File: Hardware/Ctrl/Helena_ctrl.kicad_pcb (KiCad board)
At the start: 2 copper layers, 38 x 18 mm, 41 parts, among them P1 CONN_01X06, P2 CONN_01X04, Q1 BC857C, SW1 SW_PUSH, U1 antenna-gnd, U2 nrf51822-qfax, U3 MPU-6050, Y1 16MHz

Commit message: updated control board
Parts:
- removed C10, C7: 22p, rt_device:C_0603_THERMaL_RELIEF
- removed C11, C12, C3, C4: 100n, rt_device:C_0603_THERMaL_RELIEF
- removed C5: 1p0, rt_device:C_0603_THERMaL_RELIEF
- removed C6: 1n, rt_device:C_0603_THERMaL_RELIEF
- removed C8: 2p2, rt_device:C_0603_THERMaL_RELIEF
- removed C9: 2n2, rt_device:C_0603_THERMaL_RELIEF
- removed L1: 3n3, rt_device:C_0603_THERMaL_RELIEF
- removed L2: 4n7, rt_device:C_0603_THERMaL_RELIEF
- removed L3: 10n, rt_device:C_0603_THERMaL_RELIEF
- removed Q1: BC857C, TO_SOT_Packages_SMD:SOT-23
- removed U1: antenna-gnd, rt_antennas:MML_R302.302.000
- removed Y1: 16MHz, rt_XTAL:XTAL_MT_3.2mm_x_2.5mm
- added D2: LED_BLUE, rt_device:C_0603_THERMaL_RELIEF, F.Cu at (54.1, 148.5)
- added FB2: FB, rt_device:C_0603_THERMaL_RELIEF, B.Cu at (42.4, 155.7)
- C1: value dnp -> 2u2/16
- C2: value 1p5 -> 100n
- D1: value Double_LED -> LED_RED; footprint rt_leds:Duo-Led_0603 -> rt_device:C_0603_THERMaL_RELIEF
- P2: value CONN_01X04 -> CONN_02X05; footprint rt_Pin_Header:Pin_Header_Straight_1x04_Pitch1.27mm -> rt_Pin_Header:Pin_Header_Straight_2x05_Pitch1.27mm
- U2: value nrf51822-qfax -> nrf51822-04AT_Module; footprint Housings_DFN_QFN:UQFN-48-1EP_6x6mm_Pitch0.4mm -> WT51822-S4AT
- moved C13 25.6 mm to (36.5, 150.7), turned to 180 degrees
- moved C15 25.0 mm to (36.5, 149.1), turned to 180 degrees
- moved C17 24.3 mm to (39.2, 142.1), turned to 180 degrees
- moved U3 20.8 mm to (39.5, 145.6), turned to 180 degrees
- moved FB1 19.9 mm to (39.5, 150.7), turned to 180 degrees
- moved R2 19.6 mm to (38.4, 153.4)
- moved C14 19.1 mm to (39.5, 149.1), turned to 0 degrees
- moved R1 19.1 mm to (39.2, 155.7), turned to 180 degrees
- moved C16 16.8 mm to (40.0, 153.4)
- moved R3 14.0 mm to (42.5, 150.7), turned to 0 degrees
- moved R4 12.8 mm to (54.1, 154.5), turned to 90 degrees
- moved R5 12.6 mm to (42.5, 149.1), turned to 0 degrees
- moved U2 11.7 mm to (58.8, 150.4), turned to 90 degrees
- moved P2 9.83 mm to (48.9, 143.2), turned to 270 degrees
- moved D1 8.89 mm to (54.1, 151.5), turned to 270 degrees
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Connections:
- D1 pad 1: GND -> /~LED_RED~/LED_BLUE
- P2 pad 2: /SWDCLK -> /SWDIO
- P2 pad 4: /SWDIO -> /SWDCLK
- R4 pad 1: /LED_RED -> +3V3
- R4 pad 2: Net-(D1-Pad4) -> Net-(D1-Pad2)
- R7 pad 1: /LED_BLUE -> Net-(D2-Pad1)
- R7 pad 2: Net-(D1-Pad2) -> GND
- U2 pad 1: +3V3 -> Net-(C1-Pad1)
- U2 pad 10: /VIN_ADC -> /SWDIO
- U2 pad 11: Net-(U2-Pad11) -> /SWDCLK
- U2 pad 12: +3V3 -> GND
- U2 pad 15: Net-(U2-Pad15) -> GND
- U2 pad 2: Net-(U2-Pad2) -> GND
- U2 pad 3: Net-(U2-Pad3) -> /VIN_ADC
- U2 pad 4: Net-(U2-Pad4) -> /SDA
- U2 pad 5: Net-(U2-Pad5) -> /SCL
- U2 pad 6: Net-(U2-Pad6) -> /MPU_INT
- U2 pad 7: Net-(U2-Pad7) -> /BUTTON
- U2 pad 8: Net-(U2-Pad8) -> /BDEP_RX
- U2 pad 9: Net-(U2-Pad9) -> /~LED_RED~/LED_BLUE
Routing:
- net GND: track 159.0 -> 98.3 mm, vias 75 -> 39
- net /LED_RED: track 20.9 -> 0.00 mm, vias 1 -> 0
- net +3V3: track 57.5 -> 41.9 mm
- net /~LED_RED~/LED_BLUE: track 0.00 -> 11.0 mm, vias 0 -> 1
- net Net-(D1-Pad2): track 10.6 -> 1.48 mm
- net VPP: track 10.8 -> 19.7 mm, vias 1 -> 0
- net Net-(C10-Pad1): track 8.89 -> 0.00 mm
- net /BDEP_TX: track 8.40 -> 0.00 mm, vias 1 -> 0
- net /BUTTON: track 16.8 -> 25.1 mm, vias 1 -> 3
- net Net-(D1-Pad4): track 8.04 -> 0.00 mm
- net Net-(C7-Pad1): track 7.74 -> 0.00 mm
- net /LED_BLUE: track 7.06 -> 0.00 mm, vias 1 -> 0
- net Net-(C9-Pad1): track 6.09 -> 0.00 mm
- net /SDA: track 26.3 -> 20.9 mm, vias 1 -> 0
- net /SWDCLK: track 5.44 -> 10.0 mm
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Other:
- board text added: "1"
- board text added: "10pin ARM"
- board text added: "RT1703"
- board text added: "Wireless Ctrl. Rev 2.2"
- board text removed: "RT1612"
- board text removed: "SWDIO GND SWDCLK +3V3"
- board text removed: "Wireless Ctrl. Rev 2.1"

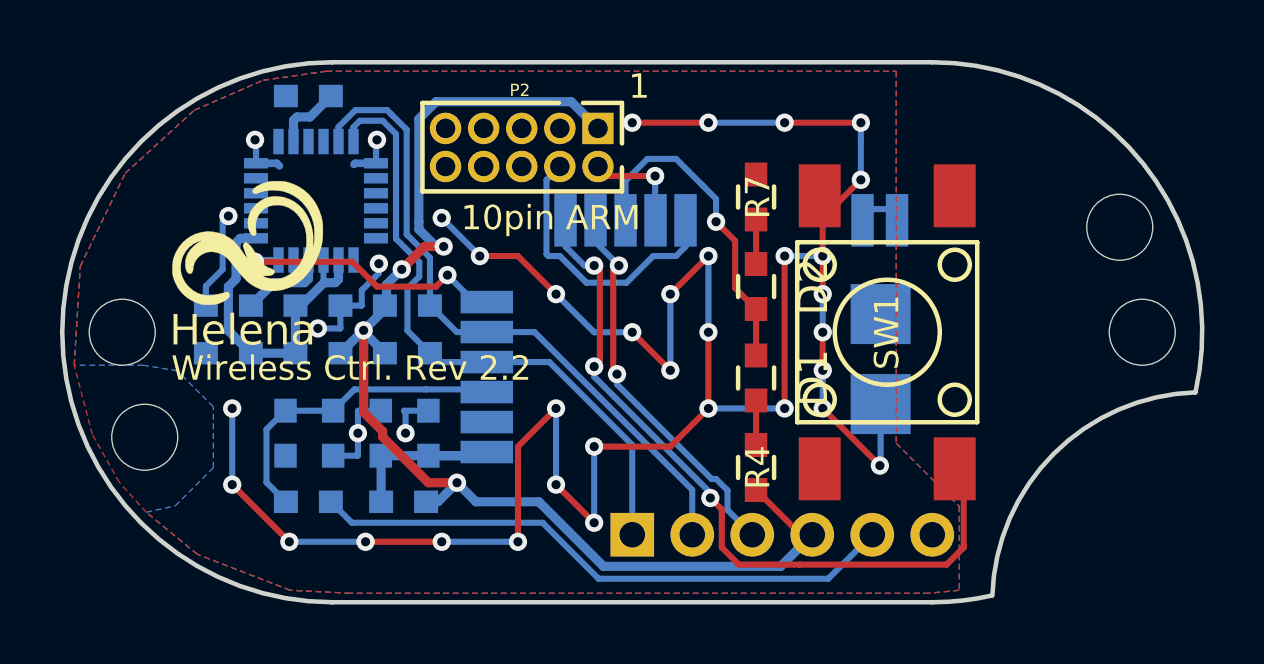
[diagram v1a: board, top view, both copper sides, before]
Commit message: Hardware update for better compatibility with KD2 style lights
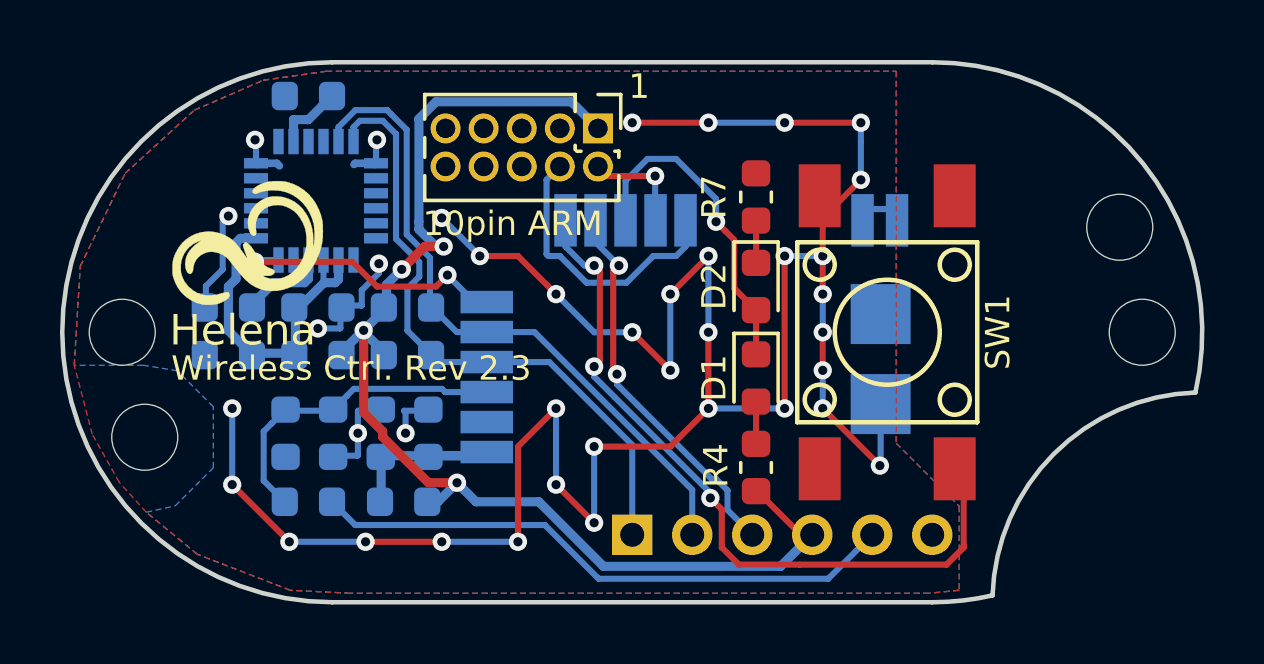
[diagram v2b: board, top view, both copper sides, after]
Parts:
- removed P1: CONN_01X06, rt_Pin_Header:Pin_Header_Straight_1x06_2.00_Pitch
- removed P2: CONN_02X05, rt_Pin_Header:Pin_Header_Straight_2x05_Pitch1.27mm
- added J1: CONN_01X06, Connector_PinHeader_2.00mm:PinHeader_1x06_P2.00mm_Vertical, B.Cu at (50.0, 156.8)
- added J2: CONN_02X05, Connector_PinHeader_1.27mm:PinHeader_2x05_P1.27mm_Vertical, F.Cu at (48.9, 143.2)
- C1, C13, C14, C15, C16, C17, C2: footprint rt_device:C_0603_THERMaL_RELIEF -> Capacitor_SMD:C_0603_1608Metric
- D1, D2: footprint rt_device:C_0603_THERMaL_RELIEF -> Diode_SMD:D_0603_1608Metric
- FB1, FB2: footprint rt_device:C_0603_THERMaL_RELIEF -> Inductor_SMD:L_0603_1608Metric
- R1, R2, R3, R4, R5, R7: footprint rt_device:C_0603_THERMaL_RELIEF -> Resistor_SMD:R_0603_1608Metric
- moved C13 0.06 mm to (36.5, 150.8)
- moved C14 0.06 mm to (39.5, 149.2)
- moved C15 0.06 mm to (36.5, 149.2)
- moved FB1 0.06 mm to (39.5, 150.8)
- moved R3 0.06 mm to (42.5, 150.8)
- moved R5 0.06 mm to (42.5, 149.2)
- renumbered U2 to A1, U3 to U1
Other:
- rule pad_to_mask_clearance: 0.2 -> 0.05
- board text added: "RT1908"
- board text added: "Wireless Ctrl. Rev 2.3"
- board text removed: "RT1703"
- board text removed: "Wireless Ctrl. Rev 2.2"
